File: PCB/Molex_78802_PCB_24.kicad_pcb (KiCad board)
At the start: 2 copper layers, 16.5 x 32.9 mm, 1 part

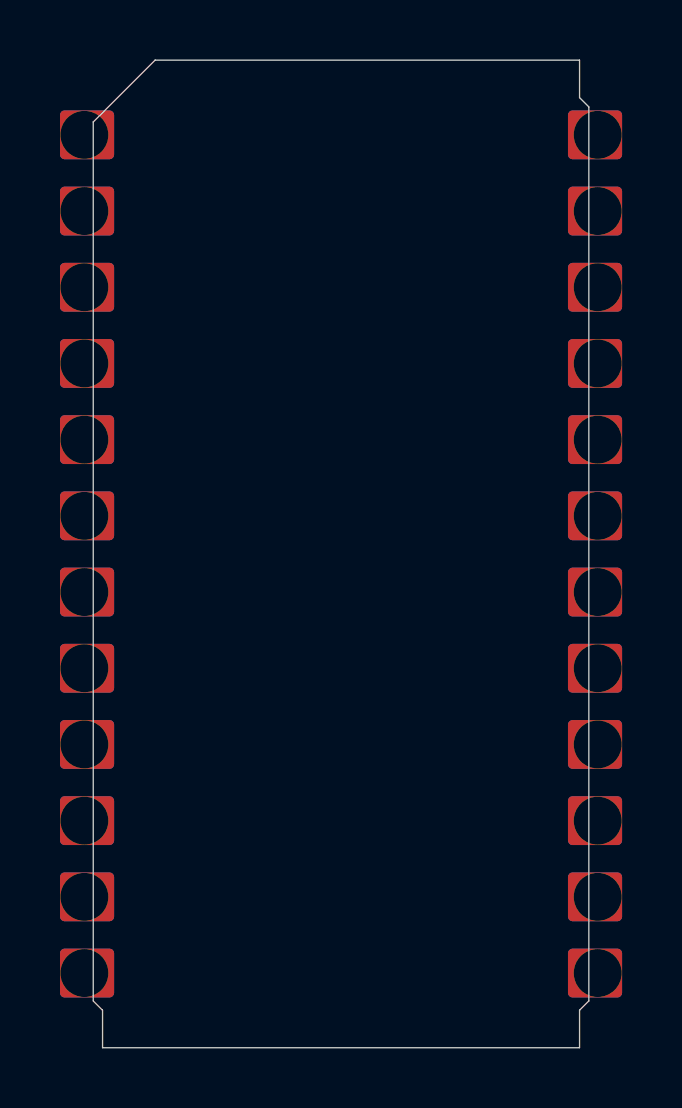
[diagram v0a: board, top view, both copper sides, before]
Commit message: improved fitment all around, simplified the pcb corners, removed junk from the scad model
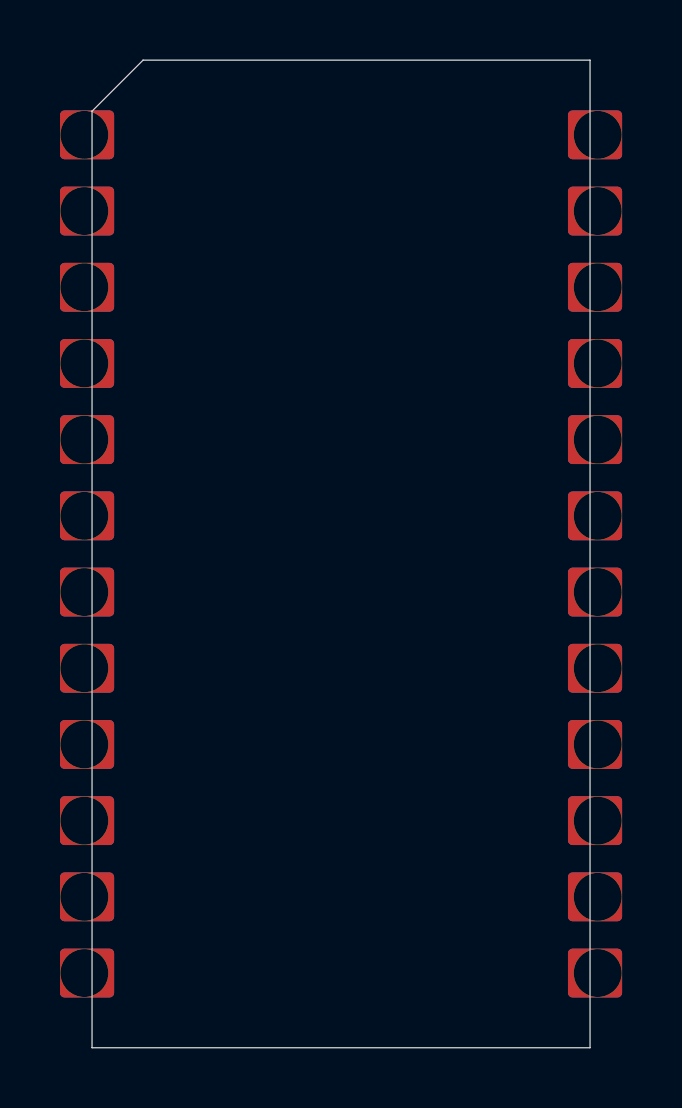
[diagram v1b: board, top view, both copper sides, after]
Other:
- board size 16.5 x 32.9 mm -> 16.6 x 32.9 mm
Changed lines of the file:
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@@
   (general
     (thickness 1.6)
-    (drawings 11)
+    (drawings 5)
     (tracks 0)
     (zones 0)
@@
     (title "Molex78802 PCB 24")
     (date 2021-05-20)
-    (rev 004)
+    (rev 005)
     (company b.kenyon.w@gmail.com)
   )
@@
     (fp_line (start -6 -14.46) (end -5.5 -14.46) (layer Dwgs.User) (width 0.01))
     (fp_line (start -6 -15.76) (end -6 -14.46) (layer Dwgs.User) (width 0.01))
-    (fp_line (start 7.2 -15.76) (end 7.2 15.76) (layer Dwgs.User) (width 0.01))
-    (fp_line (start -7.2 -15.76) (end -7.2 15.76) (layer Dwgs.User) (width 0.01))
-    (fp_line (start -7.2 -15.76) (end 7.2 -15.76) (layer Dwgs.User) (width 0.01))
-    (fp_line (start -7.2 15.76) (end 7.2 15.76) (layer Dwgs.User) (width 0.01))
-    (fp_line (start -8.255 0.0508) (end -8.255 -0.0508) (layer Dwgs.User) (width 0.002))
+    (fp_line (start 7.6 -15.76) (end 7.6 15.76) (layer Dwgs.User) (width 0.01))
+    (fp_line (start -7.6 -15.76) (end -7.6 15.76) (layer Dwgs.User) (width 0.01))
+    (fp_line (start -7.6 -15.76) (end 7.6 -15.76) (layer Dwgs.User) (width 0.01))
+    (fp_line (start -7.6 15.76) (end 7.6 15.76) (layer Dwgs.User) (width 0.01))
     (fp_poly (pts (xy 9.2156 1.9304) (xy 7.717 1.9304) (xy 7.717 0.6096) (xy 9.2156 0.6096)) (layer Top) (width 0.3048))
     (fp_poly (pts (xy 9.2156 -0.6096) (xy 7.717 -0.6096) (xy 7.717 -1.9304) (xy 9.2156 -1.9304)) (layer Top) (width 0.3048))
@@
     (fp_line (start -0.762 -19.05) (end 0.762 -19.05) (layer Eco1.User) (width 0.01))
     (fp_line (start -0.762 -16.51) (end -0.762 -19.05) (layer Eco1.User) (width 0.01))
-    (fp_line (start -7.95 16.46) (end 7.95 16.46) (layer Eco2.User) (width 0.01))
-    (fp_line (start 7.95 16.46) (end 7.95 15.21) (layer Eco2.User) (width 0.01))
-    (fp_line (start -7.95 16.46) (end -7.95 15.21) (layer Eco2.User) (width 0.01))
-    (fp_line (start 7.95 -15.21) (end 7.95 -16.46) (layer Eco2.User) (width 0.01))
-    (fp_line (start 8.26 14.9) (end 8.26 -14.9) (layer Eco2.User) (width 0.01))
-    (fp_line (start -8.26 14.9) (end -8.26 -14.4) (layer Eco2.User) (width 0.01))
-    (fp_line (start 7.95 -16.46) (end -6.2 -16.46) (layer Eco2.User) (width 0.01))
-    (fp_line (start -6.2 -16.46) (end -8.26 -14.4) (layer Eco2.User) (width 0.01))
+    (fp_line (start -8.3 16.46) (end 8.3 16.46) (layer Eco2.User) (width 0.01))
+    (fp_line (start 8.3 16.46) (end 8.3 -16.46) (layer Eco2.User) (width 0.01))
+    (fp_line (start 8.3 -16.46) (end -6.6 -16.46) (layer Eco2.User) (width 0.01))
     (fp_line (start 7.75716 15.24) (end 7.75716 10.16) (layer Dwgs.User) (width 0.01))
-    (fp_line (start 6.35 9.525) (end 6.35 12.7) (layer Dwgs.User) (width 0.05))
-    (fp_line (start 6.35 12.7) (end 7.747 12.7) (layer Dwgs.User) (width 0.05))
-    (fp_line (start 7.747 12.7) (end 7.467 12.98) (layer Dwgs.User) (width 0.05))
-    (fp_line (start 7.467 12.42) (end 7.747 12.7) (layer Dwgs.User) (width 0.05))
-    (fp_line (start 8.27 12.7) (end 8.55 12.98) (layer Dwgs.User) (width 0.05))
-    (fp_line (start 8.55 12.42) (end 8.27 12.7) (layer Dwgs.User) (width 0.05))
-    (fp_line (start 8.27 12.7) (end 9.667 12.7) (layer Dwgs.User) (width 0.05))
+    (fp_line (start 6.34 9.525) (end 6.34 12.7) (layer Dwgs.User) (width 0.05))
+    (fp_line (start 6.34 12.7) (end 7.737 12.7) (layer Dwgs.User) (width 0.05))
+    (fp_line (start 7.737 12.7) (end 7.457 12.98) (layer Dwgs.User) (width 0.05))
+    (fp_line (start 7.457 12.42) (end 7.737 12.7) (layer Dwgs.User) (width 0.05))
+    (fp_line (start 8.33 12.7) (end 8.61 12.98) (layer Dwgs.User) (width 0.05))
+    (fp_line (start 8.61 12.42) (end 8.33 12.7) (layer Dwgs.User) (width 0.05))
+    (fp_line (start 8.33 12.7) (end 9.727 12.7) (layer Dwgs.User) (width 0.05))
     (fp_line (start -5 -16.46) (end -5 -15.46) (layer Dwgs.User) (width 0.01))
     (fp_line (start -5 -15.46) (end 5 -15.46) (layer Dwgs.User) (width 0.01))
@@
     (fp_line (start -5 15.46) (end 5 15.46) (layer Dwgs.User) (width 0.01))
     (fp_line (start -5 16.46) (end 5 16.46) (layer Dwgs.User) (width 0.01))
-    (fp_line (start 7.95 -15.21) (end 8.26 -14.9) (layer Eco2.User) (width 0.01))
-    (fp_line (start -7.95 15.21) (end -8.26 14.9) (layer Eco2.User) (width 0.01))
-    (fp_line (start 7.95 15.21) (end 8.26 14.9) (layer Eco2.User) (width 0.01))
-    (fp_text user "0.7 border on bottom - 31.52 x 14.4 x 1.4 usable bottom" (at -5.5 -14.46) (layer Dwgs.User)
+    (fp_line (start -8.3 16.46) (end -8.3 -14.76) (layer Eco2.User) (width 0.01))
+    (fp_line (start -6.6 -16.46) (end -8.3 -14.76) (layer Eco2.User) (width 0.01))
+    (fp_text user "0.7 border on bottom - 31.32 x 15 x 1.4 usable bottom" (at -5.5 -14.46) (layer Dwgs.User)
       (effects (font (size 0.25 0.25) (thickness 0.02)) (justify left))
     )
@@
       (zone_connect 0))
     (model ${KIPRJMOD}/000_LOCAL.pretty/3d/Molex78802_PCB_24.step
-      (offset (xyz 0 0 -0.18))
+      (offset (xyz 0 0 -0.16))
       (scale (xyz 1 1 1))
       (rotate (xyz 0 0 90))
     )
   )
-  (gr_line (start 139.2684 114.397) (end 138.9584 114.087) (layer Edge.Cuts) (width 0.01))
-  (gr_line (start 155.1684 114.397) (end 155.4784 114.087) (layer Edge.Cuts) (width 0.01))
-  (gr_line (start 155.1684 83.977) (end 155.4784 84.287) (layer Edge.Cuts) (width 0.01))
-  (gr_line (start 139.2684 114.397) (end 139.2684 115.647) (layer Edge.Cuts) (width 0.01))
-  (gr_line (start 138.9584 84.787) (end 138.9584 114.087) (layer Edge.Cuts) (width 0.01))
-  (gr_line (start 141.0184 82.727) (end 138.9584 84.787) (layer Edge.Cuts) (width 0.01))
-  (gr_line (start 155.1684 82.727) (end 141.0184 82.727) (layer Edge.Cuts) (width 0.01))
-  (gr_line (start 155.1684 83.977) (end 155.1684 82.727) (layer Edge.Cuts) (width 0.01))
-  (gr_line (start 155.4784 114.087) (end 155.4784 84.287) (layer Edge.Cuts) (width 0.01))
-  (gr_line (start 155.1684 115.647) (end 155.1684 114.397) (layer Edge.Cuts) (width 0.01))
-  (gr_line (start 139.2684 115.647) (end 155.1684 115.647) (layer Edge.Cuts) (width 0.01))
+  (gr_line (start 155.5184 115.647) (end 155.5184 82.727) (layer Edge.Cuts) (width 0.01))
+  (gr_line (start 138.9184 84.427) (end 140.6184 82.727) (layer Edge.Cuts) (width 0.01))
+  (gr_line (start 138.9184 115.647) (end 138.9184 84.427) (layer Edge.Cuts) (width 0.01))
+  (gr_line (start 155.5184 82.727) (end 140.6184 82.727) (layer Edge.Cuts) (width 0.01))
+  (gr_line (start 138.9184 115.647) (end 155.5184 115.647) (layer Edge.Cuts) (width 0.01))
 )
